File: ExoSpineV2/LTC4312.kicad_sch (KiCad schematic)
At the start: 10 parts, among them U9 LTC4312IMS_PBF

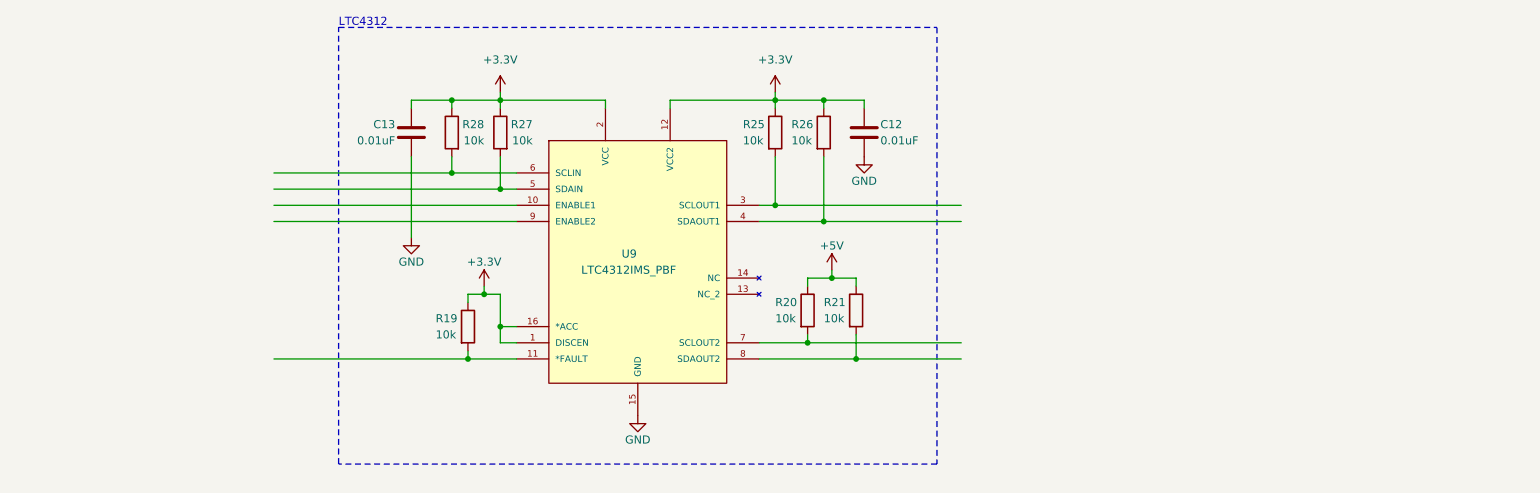
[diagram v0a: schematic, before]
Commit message: Added connections to batteries PCBs
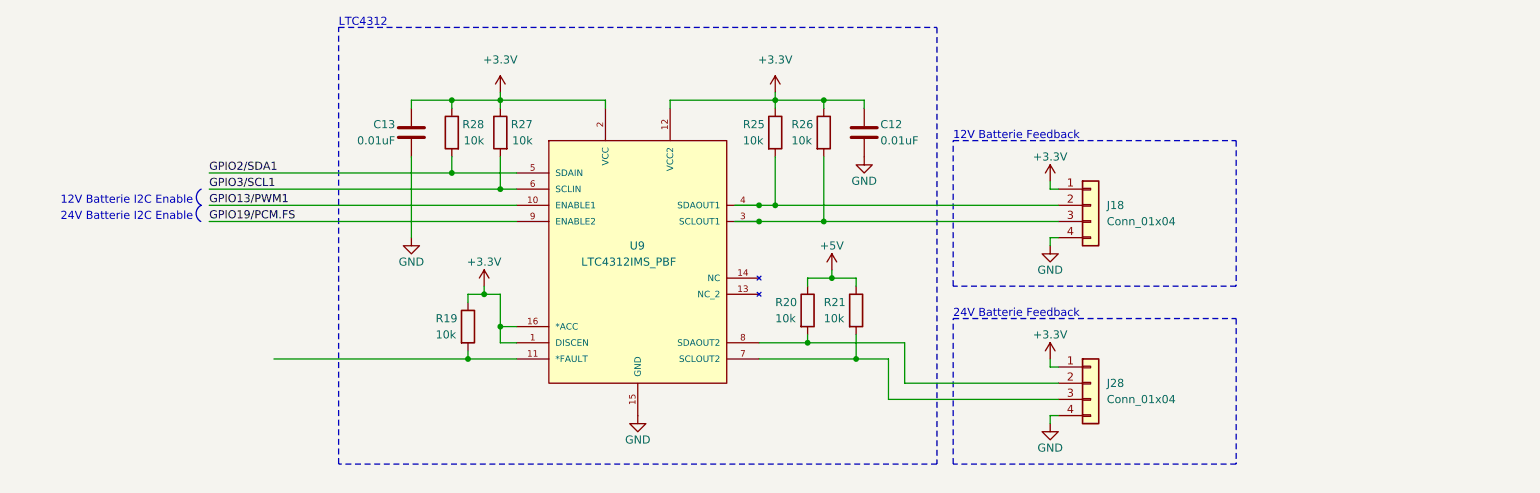
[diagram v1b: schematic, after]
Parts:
- added J18, J28: Conn_01x04, symbol Connector_Generic:Conn_01x04
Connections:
- net +3.3V: now also J18.1 (Pin_1), J28.1 (Pin_1)
- net GND: now also J18.4 (Pin_4), J28.4 (Pin_4)
- net at R21.2: now also U9.7 (SCLOUT2), J28.3 (Pin_3); no longer U9.8 (SDAOUT2)
- net at R26.2: now also U9.3 (SCLOUT1), J18.3 (Pin_3); no longer U9.4 (SDAOUT1)
- net GPIO2/SDA1: now reaches R28.2
- net GPIO2/SDA1: now also U9.5 (SDAIN); no longer U9.6 (SCLIN)
- net GPIO13/PWM1: now reaches U9.10 (ENABLE1)
- net at R25.2: now also U9.4 (SDAOUT1), J18.2 (Pin_2); no longer U9.3 (SCLOUT1)
- net GPIO3/SCL1: now reaches R27.2
- net GPIO3/SCL1: now also U9.6 (SCLIN); no longer U9.5 (SDAIN)
- net at R20.2: now also U9.8 (SDAOUT2), J28.2 (Pin_2); no longer U9.7 (SCLOUT2)
- net GPIO19/PCM.FS: now reaches U9.9 (ENABLE2)
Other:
- note added: "12V Batterie Feedback"
- note added: "12V Batterie I2C Enable"
- note added: "24V Batterie Feedback"
- note added: "24V Batterie I2C Enable"

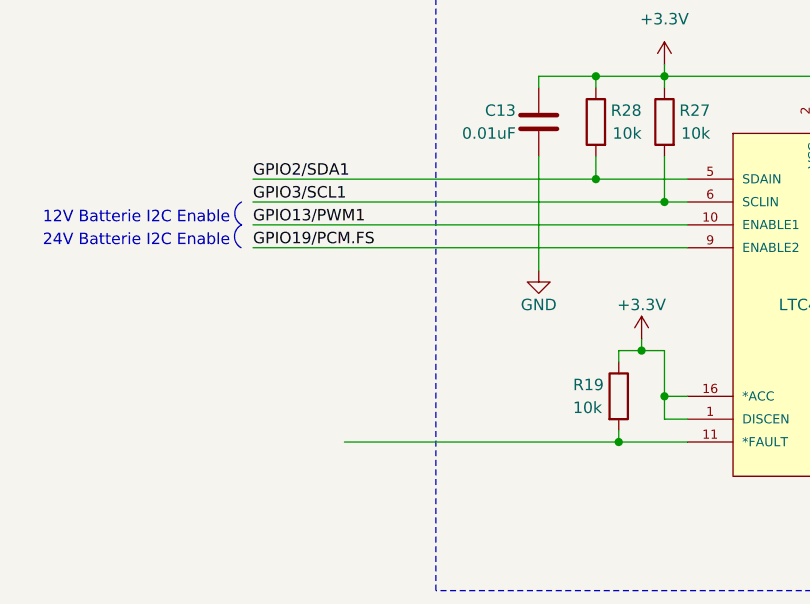
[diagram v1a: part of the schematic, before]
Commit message: added connection type for GPS
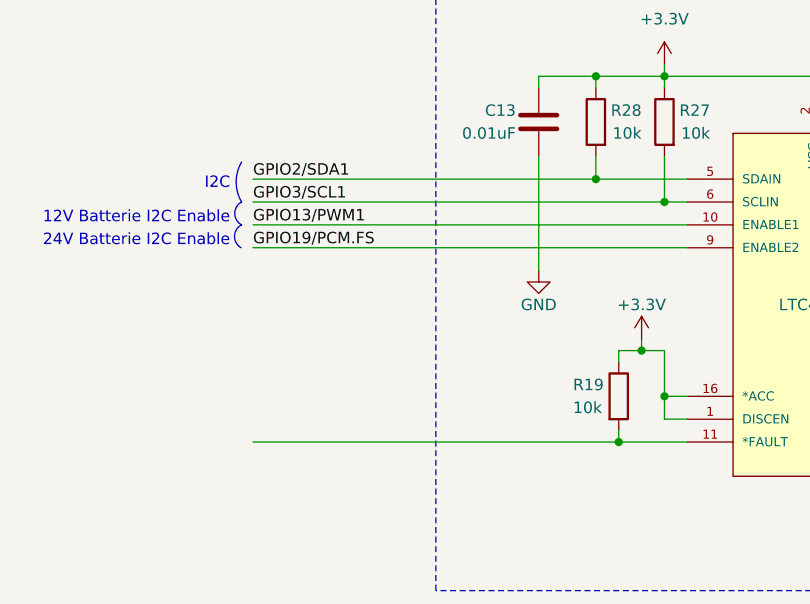
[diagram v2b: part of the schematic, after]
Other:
- note added: "I2C"
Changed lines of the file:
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@@
     (stroke (width 0) (type default))
   )
-  (wire (pts (xy 64.77 109.22) (xy 95.25 109.22))
+  (wire (pts (xy 54.61 109.22) (xy 95.25 109.22))
     (stroke (width 0) (type default))
   )
@@
     (fill (type none))
   )
+  (arc (start 53.34 82.55) (mid 52.7428 80.3275) (end 53.34 78.105)
+    (stroke (width 0) (type default) (color 132 132 132 1))
+    (fill (type none))
+  )
   (text "12V Batterie I2C Enable" (at 52.07 85.09 0)
     (effects (font (size 1.27 1.27) (color 132 132 132 1)) (justify right bottom))
@@
     (effects (font (size 1.27 1.27)) (justify left bottom))
   )
+  (text "I2C" (at 52.07 81.28 0)
+    (effects (font (size 1.27 1.27) (color 132 132 132 1)) (justify right bottom))
+  )
   (text "LTC4312" (at 74.93 57.15 0)

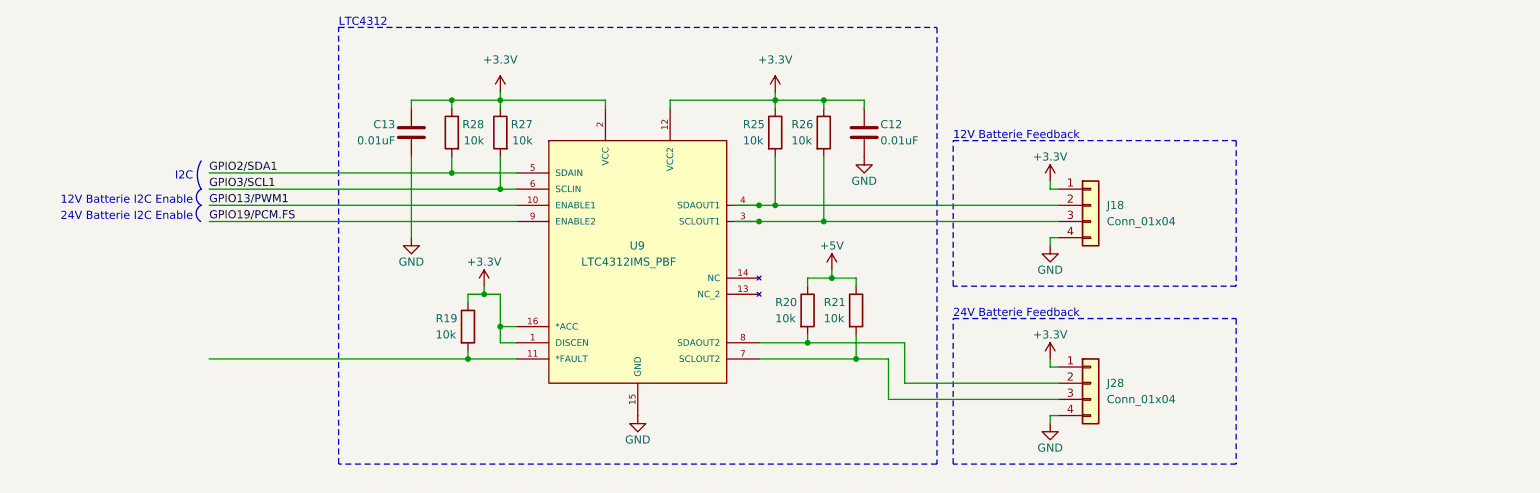
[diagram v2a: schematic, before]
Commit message: modified battery feedback control (switch)
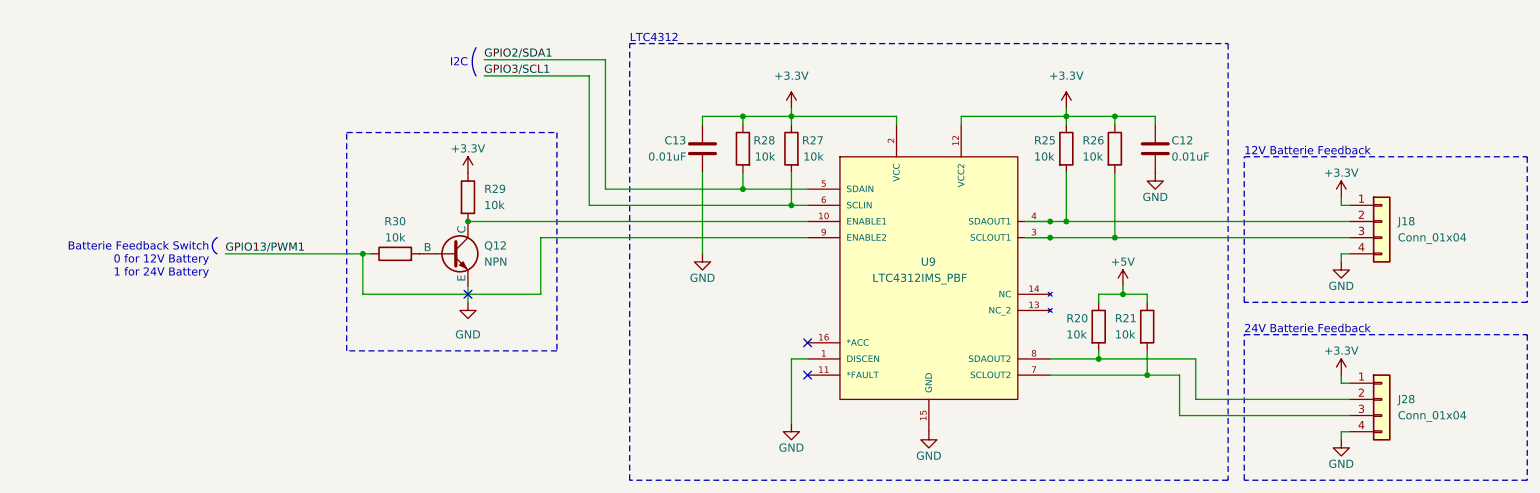
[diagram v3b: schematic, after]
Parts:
- removed R19: 10k, symbol Device:R
- added Q12: NPN, symbol Simulation_SPICE:NPN
- added R29, R30: 10k, symbol Device:R
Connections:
- net GPIO19/PCM.FS is gone; now on net GPIO13/PWM1: U9.9 (ENABLE2)
- net +3.3V: now also R29.1; no longer U9.1 (DISCEN), U9.16 (*ACC)
- net GND: now also U9.1 (DISCEN), Q12.3 (E)
- net GPIO13/PWM1: now also R30.1; no longer U9.10 (ENABLE1)
- new net: Q12.2 (B), R30.2
- new net: Q12.1 (C), R29.2, U9.10 (ENABLE1)
- no-connect marks 0 -> 3
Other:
- note added: "Batterie Feedback Switch 0 for 12V Battery 1 for 24V Battery"
- note removed: "12V Batterie I2C Enable"
- note removed: "24V Batterie I2C Enable"
- moved on the sheet: C12, C13, J18, J28, R20, R21, R25, R26, R27, R28, U9

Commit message: chose 10k resistors on JLCPCB (datasheets & footprints)
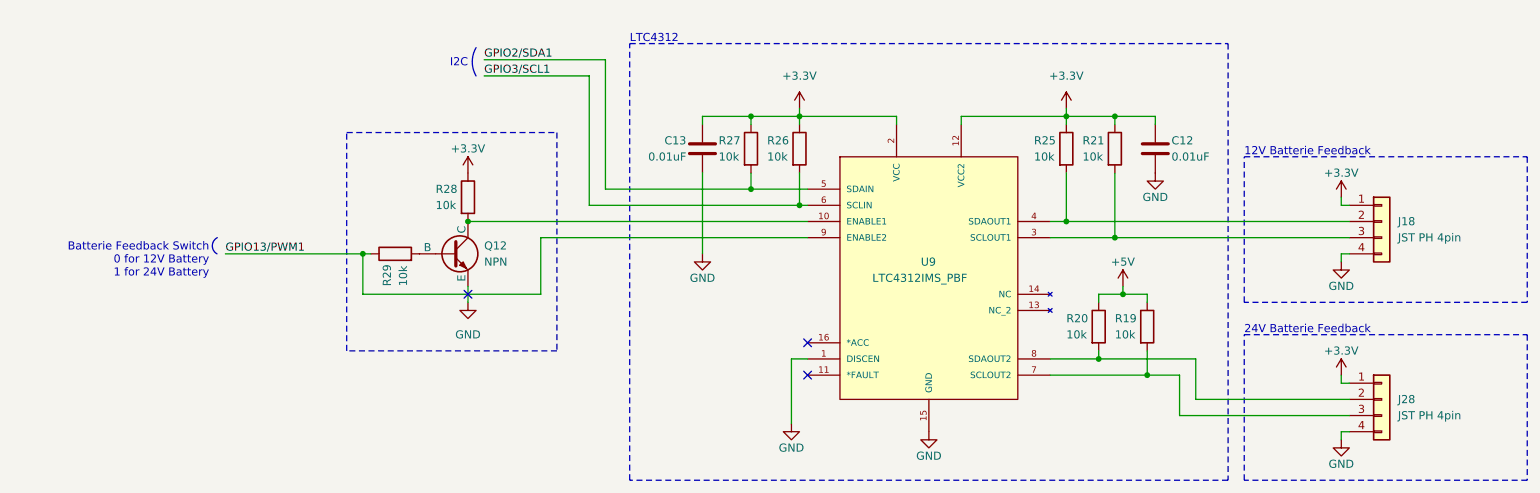
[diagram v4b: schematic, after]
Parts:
- removed R30: 10k, symbol Device:R
- added R19: 10k, Resistor_SMD:R_0402_1005Metric, symbol Device:R
- J18, J28: value Conn_01x04 -> JST PH 4pin; footprint (none) -> Connector_JST:JST_PH_B4B-PH-K_1x04_P2.00mm_Vertical
- R20, R21, R25, R26, R27, R28, R29: footprint (none) -> Resistor_SMD:R_0402_1005Metric; JLCPCB (none) -> https://jlcpcb.com/partdetail/26487-0402WGF1002TCE/C25744
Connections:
- net +3.3V: now also R21.1; no longer R29.1
- net +5V: now also R19.1; no longer R21.1
- net GPIO13/PWM1: now also R29.1
- net GPIO2/SDA1: now also R27.2; no longer R28.2
- net GPIO3/SCL1: now also R26.2; no longer R27.2
- net at J28.3 (Pin_3), U9.7 (SCLOUT2): now also R19.2; no longer R21.2
- net at Q12.2 (B): now also R29.2
- net at J18.3 (Pin_3), U9.3 (SCLOUT1): now also R21.2; no longer R26.2
- net at Q12.1 (C), U9.10 (ENABLE1): now also R28.2; no longer R29.2

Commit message: chose resistors and capacitors
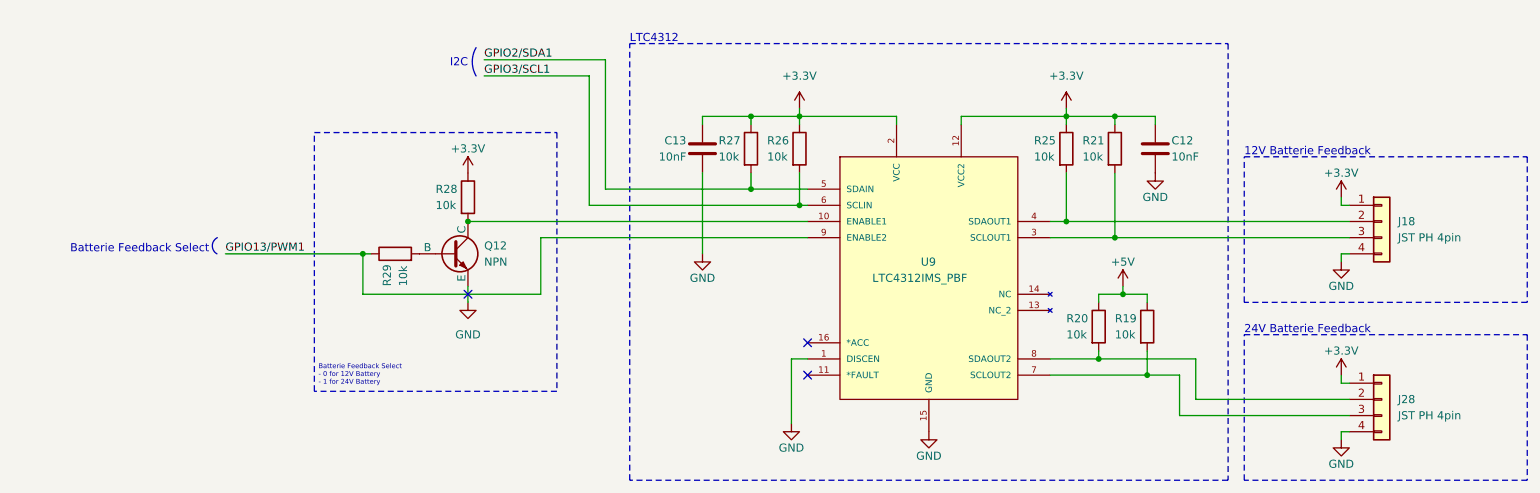
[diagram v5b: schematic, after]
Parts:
- C12, C13: value 0.01uF -> 10nF; footprint (none) -> Capacitor_SMD:C_0805_2012Metric; JLCPCB (none) -> https://jlcpcb.com/partdetail/2062-CL21B103KBANNNC/C1710
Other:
- note added: "Batterie Feedback Select"
- note removed: "Batterie Feedback Switch 0 for 12V Battery 1 for 24V Battery"
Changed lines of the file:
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@@
     (stroke (width 0) (type default))
   )
-  (rectangle (start 76.2 73.66) (end 109.22 107.95)
+  (rectangle (start 71.12 73.66) (end 109.22 114.3)
     (stroke (width 0) (type dash) (color 0 194 0 1))
     (fill (type none))
@@
     (fill (type none))
   )
-  (text "Batterie Feedback Switch\n0 for 12V Battery\n1 for 24V Battery"
-    (at 54.61 96.52 0)
+  (text_box "Batterie Feedback Select\n- 0 for 12V Battery\n- 1 for 24V Battery"
+    (at 71.12 109.22 0) (size 20.32 5.08)
+    (stroke (width -0.0001) (type default))
+    (fill (type color) (color 255 229 191 1))
+    (effects (font (size 0.762 0.762)) (justify left top))
+  )
+  (text "Batterie Feedback Select" (at 54.61 92.71 0)
     (effects (font (size 1.27 1.27) (color 132 132 132 1)) (justify right bottom))
   )
@@
       (effects (font (size 1.27 1.27)) (justify left))
     )
-    (property "Value" "0.01uF" (at 129.54 77.47 0)
-      (effects (font (size 1.27 1.27)) (justify left))
-    )
-    (property "Footprint" "" (at 131.1148 80.01 0)
-      (effects (font (size 1.27 1.27)) hide)
-    )
-    (property "Datasheet" "~" (at 132.08 76.2 0)
+    (property "Value" "10nF" (at 129.54 77.47 0)
+      (effects (font (size 1.27 1.27)) (justify left))
+    )
+    (property "Footprint" "Capacitor_SMD:C_0805_2012Metric" (at 131.1148 80.01 0)
+      (effects (font (size 1.27 1.27)) hide)
+    )
+    (property "Datasheet" "https://wmsc.lcsc.com/wmsc/upload/file/pdf/v2/lcsc/2304140030_Samsung-Electro-Mechanics-CL21B103KBANNNC_C1710.pdf" (at 132.08 76.2 0)
+      (effects (font (size 1.27 1.27)) hide)
+    )
+    (property "JLCPCB" "https://jlcpcb.com/partdetail/2062-CL21B103KBANNNC/C1710" (at 132.08 76.2 0)
       (effects (font (size 1.27 1.27)) hide)
     )
@@
         (path "/e63e39d7-6ac0-4ffd-8aa3-1841a4541b55/20814431-03eb-459e-9e71-9431fed06066"
           (reference "#PWR052") (unit 1)
-        )
-      )
-    )
-  )
-  (symbol (lib_id "Device:C") (at 203.2 76.2 0) (unit 1)
-    (in_bom yes) (on_board yes) (dnp no)
-    (property "Reference" "C12" (at 205.74 74.93 0)
-      (effects (font (size 1.27 1.27)) (justify left))
-    )
-    (property "Value" "0.01uF" (at 205.74 77.47 0)
-      (effects (font (size 1.27 1.27)) (justify left))
-    )
-    (property "Footprint" "" (at 204.1652 80.01 0)
-      (effects (font (size 1.27 1.27)) hide)
-    )
-    (property "Datasheet" "~" (at 203.2 76.2 0)
-      (effects (font (size 1.27 1.27)) hide)
-    )
-    (pin "1")
-    (pin "2")
-    (instances
-      (project "ExospineV2"
-        (path "/e63e39d7-6ac0-4ffd-8aa3-1841a4541b55/20814431-03eb-459e-9e71-9431fed06066"
-          (reference "C12") (unit 1)
         )
       )
@@
         )
       )
+    )
+  )
+  (symbol (lib_id "Device:C") (at 203.2 76.2 0) (unit 1)
+    (in_bom yes) (on_board yes) (dnp no)
+    (property "Reference" "C12" (at 205.74 74.93 0)
+      (effects (font (size 1.27 1.27)) (justify left))
+    )
+    (property "Value" "10nF" (at 205.74 77.47 0)
+      (effects (font (size 1.27 1.27)) (justify left))
+    )
+    (property "Footprint" "Capacitor_SMD:C_0805_2012Metric" (at 204.1652 80.01 0)
+      (effects (font (size 1.27 1.27)) hide)
+    )
+    (property "Datasheet" "https://wmsc.lcsc.com/wmsc/upload/file/pdf/v2/lcsc/2304140030_Samsung-Electro-Mechanics-CL21B103KBANNNC_C1710.pdf" (at 203.2 76.2 0)
+      (effects (font (size 1.27 1.27)) hide)
+    )
+    (property "JLCPCB" "https://jlcpcb.com/partdetail/2062-CL21B103KBANNNC/C1710" (at 203.2 76.2 0)
+      (effects (font (size 1.27 1.27)) hide)
+    )
+    (pin "1")
+    (pin "2")
+    (instances
+      (project "ExospineV2"
+        (path "/e63e39d7-6ac0-4ffd-8aa3-1841a4541b55/20814431-03eb-459e-9e71-9431fed06066"
+          (reference "C12") (unit 1)
+        )
+      )

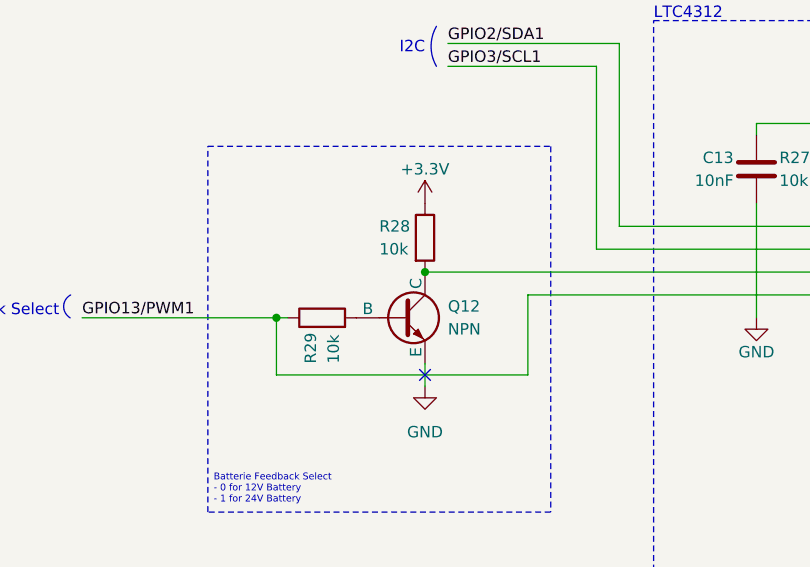
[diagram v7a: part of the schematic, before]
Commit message: changement de un peu de librairies de parts, finition du premier PCB
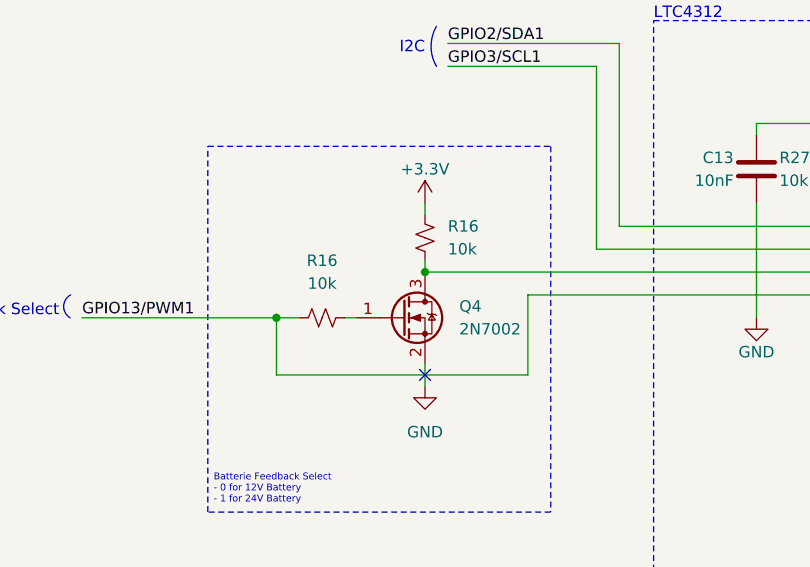
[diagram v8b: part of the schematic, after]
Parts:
- removed Q12: NPN, symbol Simulation_SPICE:NPN
- removed R28, R29: 10k, Resistor_SMD:R_0402_1005Metric, symbol Device:R
- added Q4: 2N7002, Package_TO_SOT_SMD:SOT-23, symbol Transistor_FET:2N7002
- added R16 (x2): 10k, Resistor_SMD:R_0805_2012Metric_Pad1.20x1.40mm_HandSolder, symbol Device:R_Small_US
- U9: footprint LTC4312IMS_PBF:MSOP-16_MS -> LTC4312CMS:MSOP-16_MS_LIT; JLCPCB (none) -> https://jlcpcb.com/partdetail/AnalogDevices-LTC4312CMSPBF/C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
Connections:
- net +3.3V: now also R16.1
- net GND: now also Q4.2 (S)
- net GPIO13/PWM1: now also R16.2
- net at U9.10 (ENABLE1): now also Q4.3 (D), R16.2
- new net: Q4.1 (G), R16.1
